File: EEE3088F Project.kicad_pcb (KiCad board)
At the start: 2 copper layers, 56 parts, among them J1 Conn_02x16_Odd_Even, J2 Battery IN JST, J3 USB_C_Receptacle_PowerOnly_24P, M1Control1 DRV8837, M2Control1 DRV8837, M3Control1 DRV8837, M4Control1 DRV8837, Q1 AO3400A, U1 TP4056-42-ESOP8, U2 TPS62160DGK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

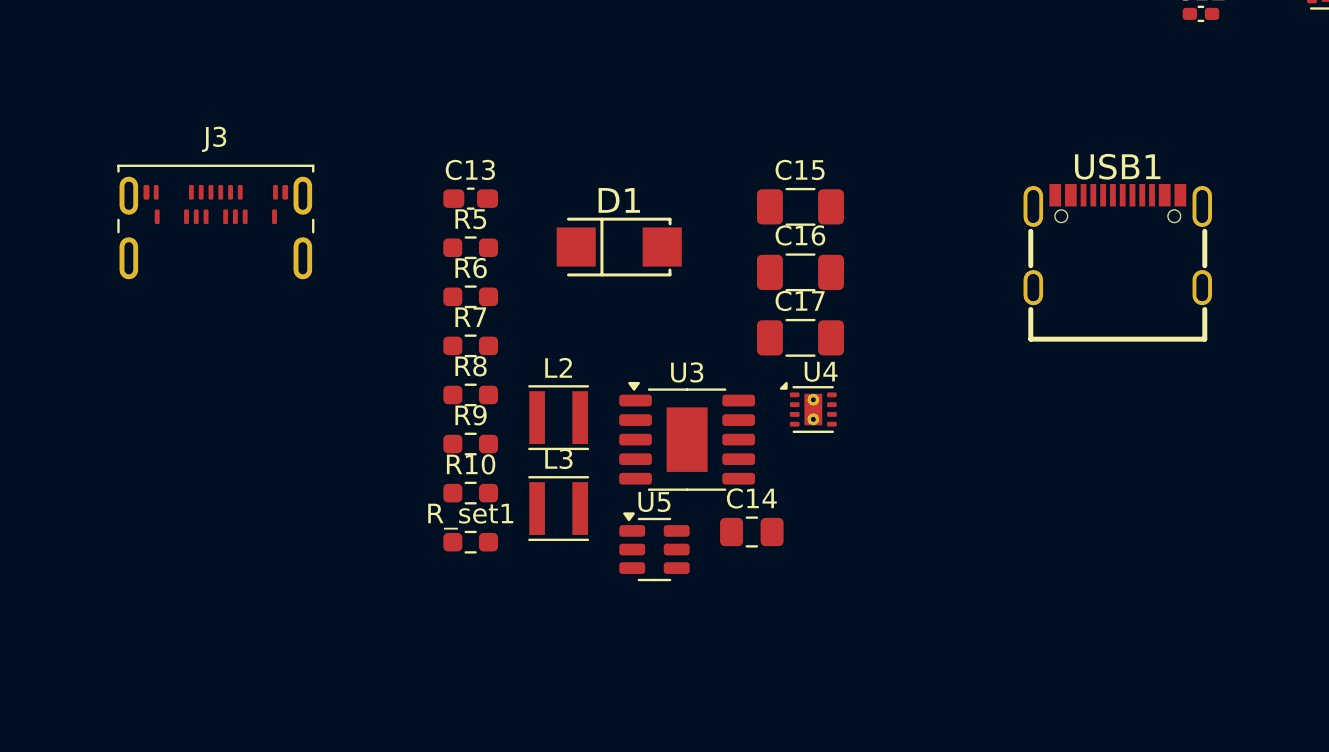
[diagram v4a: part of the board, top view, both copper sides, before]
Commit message: added custom symbol and placed usbc and schottky custom footprints into custom footprints.pretty
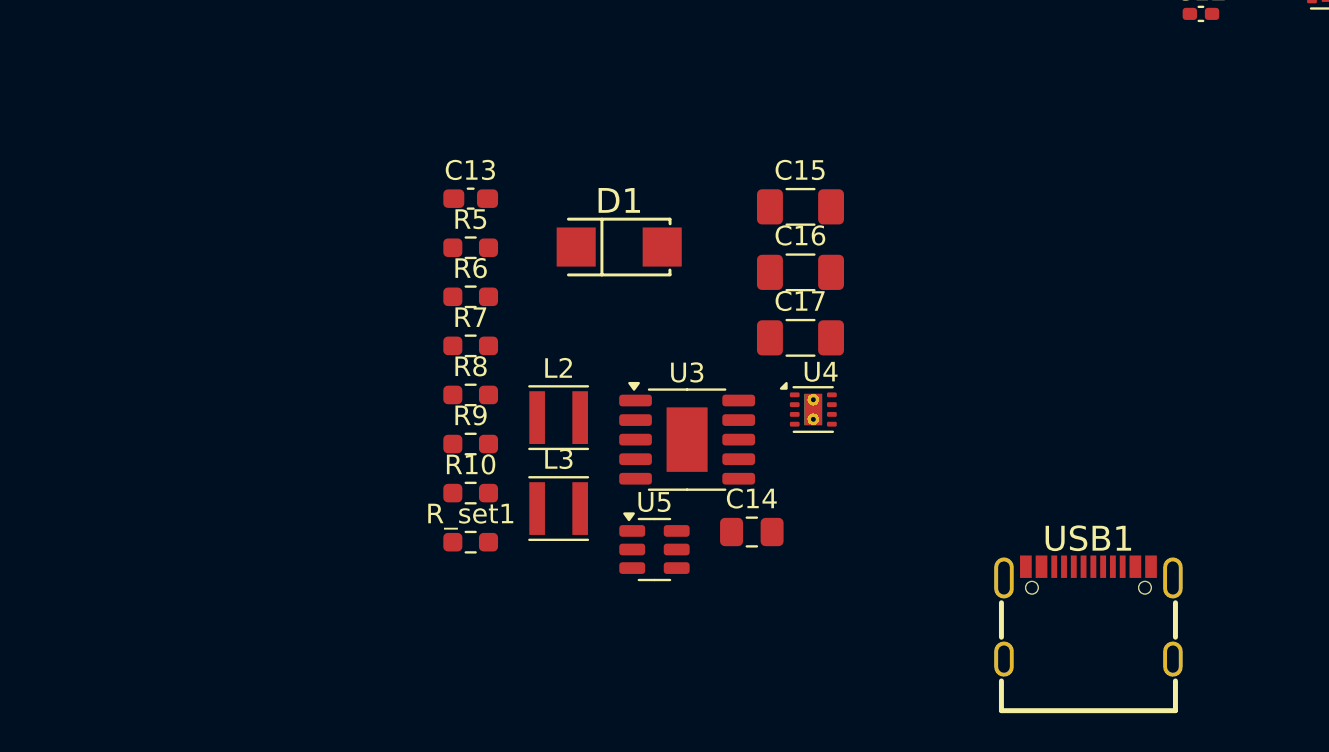
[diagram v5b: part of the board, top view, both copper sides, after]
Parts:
- removed J3: USB_C_Receptacle_PowerOnly_24P, Connector_USB:USB_C_Receptacle_Amphenol_124019772112A
- D1: footprint SMA_L4.3-W2.6-LS5.2-RD:SMA_L4.3-W2.6-LS5.2-RD -> Custom Footprints:SMA_L4.3-W2.6-LS5.2-RD
- USB1: footprint TYPE-C16PIN__:USB-C-SMD_TYPE-C16PIN -> Custom Footprints:USB-C-SMD_TYPE-C16PIN
- moved USB1 19.1 mm to (128.2, 128.6)

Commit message: Cleaned up battery charging circuit and added Battery, 3V3_out and 5V_out labels to motherboard connection
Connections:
- net Net-(R5-Pad1) renamed /VBUS_USBC
- net Net-(U3-CC1) renamed /CC1
- net Net-(U3-CC2) renamed /CC2
- C14 pad 1: 5V -> /5V_out
- C15 pad 1: 3V3 -> /3V3_out
- C17 pad 1: 5V -> /5V_out
- D1 pad 1: 5V -> /5V_out
- J1 pad 14: unconnected-(J1-Pin_14-Pad14) -> VBatt
- J1 pad 18: unconnected-(J1-Pin_18-Pad18) -> /3V3_out
- J1 pad 20: unconnected-(J1-Pin_20-Pad20) -> /5V_out
- L2 pad 2: 3V3 -> /3V3_out
- R7 pad 2: 3V3 -> /3V3_out
- R9 pad 1: 5V -> /5V_out
- U4 pad 2: 5V -> /5V_out
- U4 pad 3: 5V -> /5V_out
- U4 pad 6: 3V3 -> /3V3_out
- USB1 pad 1: unconnected-(USB1-SHELL-Pad1) -> GND
- USB1 pad 2: unconnected-(USB1-SHELL-Pad2) -> GND
- USB1 pad 3: unconnected-(USB1-SHELL-Pad3) -> GND
- USB1 pad 4: unconnected-(USB1-SHELL-Pad4) -> GND
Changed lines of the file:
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@@
 	(net 35 "/FAST_CHRG_CNTRL")
 	(net 36 "Net-(D2-A)")
-	(net 37 "unconnected-(J1-Pin_14-Pad14)")
-	(net 38 "unconnected-(J1-Pin_20-Pad20)")
+	(net 37 "/5V_out")
+	(net 38 "/3V3_out")
 	(net 39 "unconnected-(J1-Pin_12-Pad12)")
 	(net 40 "unconnected-(J1-Pin_25-Pad25)")
 	(net 41 "unconnected-(J1-Pin_22-Pad22)")
 	(net 42 "unconnected-(J1-Pin_21-Pad21)")
-	(net 43 "unconnected-(J1-Pin_18-Pad18)")
+	(net 43 "/VBUS_USBC")
 	(net 44 "unconnected-(J1-Pin_19-Pad19)")
 	(net 45 "unconnected-(J1-Pin_15-Pad15)")
@@
 	(net 53 "VBUS")
 	(net 54 "Net-(U3-VDD)")
-	(net 55 "5V")
-	(net 56 "3V3")
+	(net 55 "/CC2")
+	(net 56 "/CC1")
 	(net 57 "Net-(U4-SW)")
 	(net 58 "Net-(D1-A)")
@@
 	(net 68 "unconnected-(U3-DP-Pad4)")
 	(net 69 "unconnected-(U5-NC-Pad6)")
-	(net 70 "Net-(R5-Pad1)")
-	(net 71 "Net-(U3-CC2)")
-	(net 72 "Net-(U3-CC1)")
-	(net 73 "unconnected-(USB1-SBU1-PadA8)")
-	(net 74 "unconnected-(USB1-DP2-PadB6)")
-	(net 75 "unconnected-(USB1-SBU2-PadB8)")
-	(net 76 "unconnected-(USB1-DN2-PadB7)")
-	(net 77 "unconnected-(USB1-SHELL-Pad3)")
-	(net 78 "unconnected-(USB1-DP1-PadA6)")
-	(net 79 "unconnected-(USB1-DN1-PadA7)")
-	(net 80 "unconnected-(USB1-SHELL-Pad4)")
-	(net 81 "unconnected-(USB1-SHELL-Pad2)")
-	(net 82 "unconnected-(USB1-SHELL-Pad1)")
+	(net 70 "unconnected-(USB1-SBU1-PadA8)")
+	(net 71 "unconnected-(USB1-DP2-PadB6)")
+	(net 72 "unconnected-(USB1-SBU2-PadB8)")
+	(net 73 "unconnected-(USB1-DN2-PadB7)")
+	(net 74 "unconnected-(USB1-DP1-PadA6)")
+	(net 75 "unconnected-(USB1-DN1-PadA7)")
 	(footprint "Package_TO_SOT_SMD:SOT-23"
 		(layer "F.Cu")
@@
 			(layers "F.Cu" "F.Mask" "F.Paste")
 			(roundrect_rratio 0.25)
-			(net 71 "Net-(U3-CC2)")
+			(net 55 "/CC2")
 			(pinfunction "CC2")
 			(pintype "bidirectional")
@@
 			(layers "F.Cu" "F.Mask" "F.Paste")
 			(roundrect_rratio 0.25)
-			(net 72 "Net-(U3-CC1)")
+			(net 56 "/CC1")
 			(pinfunction "CC1")
 			(pintype "bidirectional")
@@
 			(layers "F.Cu" "F.Mask" "F.Paste")
 			(roundrect_rratio 0.25)
-			(net 56 "3V3")
+			(net 38 "/3V3_out")
 			(pintype "passive")
 		)
@@
 			(layers "F.Cu" "F.Mask" "F.Paste")
 			(roundrect_rratio 0.25)
-			(net 55 "5V")
+			(net 37 "/5V_out")
 			(pinfunction "VIN")
 			(pintype "power_in")
@@
 			(layers "F.Cu" "F.Mask" "F.Paste")
 			(roundrect_rratio 0.25)
-			(net 55 "5V")
+			(net 37 "/5V_out")
 			(pinfunction "EN")
 			(pintype "input")
@@
 			(layers "F.Cu" "F.Mask" "F.Paste")
 			(roundrect_rratio 0.25)
-			(net 56 "3V3")
+			(net 38 "/3V3_out")
 			(pinfunction "VOS")
 			(pintype "input")
@@
 			(layers "F.Cu" "F.Mask" "F.Paste")
 			(roundrect_rratio 0.188679)
-			(net 55 "5V")
+			(net 37 "/5V_out")
 			(pintype "passive")
 		)
@@
 			(size 2 2)
 			(layers "F.Cu" "F.Mask" "F.Paste")
-			(net 55 "5V")
+			(net 37 "/5V_out")
 			(pinfunction "K")
 			(pintype "passive")
@@
 			(size 0.8 2.7)
 			(layers "F.Cu" "F.Mask" "F.Paste")
-			(net 56 "3V3")
+			(net 38 "/3V3_out")
 			(pinfunction "2")
 			(pintype "passive")
@@
 			(layers "*.Cu" "*.Mask")
 			(remove_unused_layers no)
-			(net 37 "unconnected-(J1-Pin_14-Pad14)")
+			(net 3 "VBatt")
 			(pinfunction "Pin_14")
 			(pintype "passive")
@@
 			(layers "*.Cu" "*.Mask")
 			(remove_unused_layers no)
-			(net 43 "unconnected-(J1-Pin_18-Pad18)")
+			(net 38 "/3V3_out")
 			(pinfunction "Pin_18")
 			(pintype "passive")
@@
 			(layers "*.Cu" "*.Mask")
 			(remove_unused_layers no)
-			(net 38 "unconnected-(J1-Pin_20-Pad20)")
+			(net 37 "/5V_out")
 			(pinfunction "Pin_20")
 			(pintype "passive")
@@
 			(layers "F.Cu" "F.Mask" "F.Paste")
 			(roundrect_rratio 0.212766)
-			(net 55 "5V")
+			(net 37 "/5V_out")
 			(pintype "passive")
 		)
@@
 			(layers "F.Cu" "F.Mask" "F.Paste")
 			(roundrect_rratio 0.25)
-			(net 55 "5V")
+			(net 37 "/5V_out")
 			(pintype "passive")
 		)
@@
 			(layers "F.Cu" "F.Mask" "F.Paste")
 			(roundrect_rratio 0.25)
-			(net 70 "Net-(R5-Pad1)")
+			(net 43 "/VBUS_USBC")
 			(pintype "passive")
 		)
@@
 			(layers "F.Cu" "F.Mask" "F.Paste")
 			(roundrect_rratio 0.188679)
-			(net 56 "3V3")
+			(net 38 "/3V3_out")
 			(pintype "passive")
 		)
@@
 			(layers "*.Cu" "*.Mask")
 			(remove_unused_layers no)
-			(net 82 "unconnected-(USB1-SHELL-Pad1)")
+			(net 1 "GND")
 			(pinfunction "SHELL")
 			(pintype "unspecified")
@@
 			(layers "*.Cu" "*.Mask")
 			(remove_unused_layers no)
-			(net 81 "unconnected-(USB1-SHELL-Pad2)")
+			(net 1 "GND")
 			(pinfunction "SHELL")
 			(pintype "unspecified")
@@
 			(layers "*.Cu" "*.Mask")
 			(remove_unused_layers no)
-			(net 77 "unconnected-(USB1-SHELL-Pad3)")
+			(net 1 "GND")
 			(pinfunction "SHELL")
 			(pintype "unspecified")
@@
 			(layers "*.Cu" "*.Mask")
 			(remove_unused_layers no)
-			(net 80 "unconnected-(USB1-SHELL-Pad4)")
+			(net 1 "GND")
 			(pinfunction "SHELL")
 			(pintype "unspecified")
@@
 			(size 0.6 1.15)
 			(layers "F.Cu" "F.Mask" "F.Paste")
-			(net 70 "Net-(R5-Pad1)")
+			(net 43 "/VBUS_USBC")
 			(pinfunction "VBUS")
 			(pintype "unspecified")
@@
 			(size 0.3 1.15)
 			(layers "F.Cu" "F.Mask" "F.Paste")
-			(net 72 "Net-(U3-CC1)")
+			(net 56 "/CC1")
 			(pinfunction "CC1")
 			(pintype "unspecified")
@@
 			(size 0.3 1.15)
 			(layers "F.Cu" "F.Mask" "F.Paste")
-			(net 78 "unconnected-(USB1-DP1-PadA6)")
+			(net 74 "unconnected-(USB1-DP1-PadA6)")
 			(pinfunction "DP1")
 			(pintype "unspecified")
@@
 			(size 0.3 1.15)
 			(layers "F.Cu" "F.Mask" "F.Paste")
-			(net 79 "unconnected-(USB1-DN1-PadA7)")
+			(net 75 "unconnected-(USB1-DN1-PadA7)")
 			(pinfunction "DN1")
 			(pintype "unspecified")
@@
 			(size 0.3 1.15)
 			(layers "F.Cu" "F.Mask" "F.Paste")
-			(net 73 "unconnected-(USB1-SBU1-PadA8)")
+			(net 70 "unconnected-(USB1-SBU1-PadA8)")
 			(pinfunction "SBU1")
 			(pintype "unspecified")
@@
 			(size 0.6 1.15)
 			(layers "F.Cu" "F.Mask" "F.Paste")
-			(net 70 "Net-(R5-Pad1)")
+			(net 43 "/VBUS_USBC")
 			(pinfunction "VBUS")
 			(pintype "unspecified")
@@
 			(size 0.3 1.15)
 			(layers "F.Cu" "F.Mask" "F.Paste")
-			(net 71 "Net-(U3-CC2)")
+			(net 55 "/CC2")
 			(pinfunction "CC2")
 			(pintype "unspecified")
@@
 			(size 0.3 1.15)
 			(layers "F.Cu" "F.Mask" "F.Paste")
-			(net 74 "unconnected-(USB1-DP2-PadB6)")
+			(net 71 "unconnected-(USB1-DP2-PadB6)")
 			(pinfunction "DP2")
 			(pintype "unspecified")
@@
 			(size 0.3 1.15)
 			(layers "F.Cu" "F.Mask" "F.Paste")
-			(net 76 "unconnected-(USB1-DN2-PadB7)")
+			(net 73 "unconnected-(USB1-DN2-PadB7)")
 			(pinfunction "DN2")
 			(pintype "unspecified")
@@
 			(size 0.3 1.15)
 			(layers "F.Cu" "F.Mask" "F.Paste")
-			(net 75 "unconnected-(USB1-SBU2-PadB8)")
+			(net 72 "unconnected-(USB1-SBU2-PadB8)")
 			(pinfunction "SBU2")
 			(pintype "unspecified")

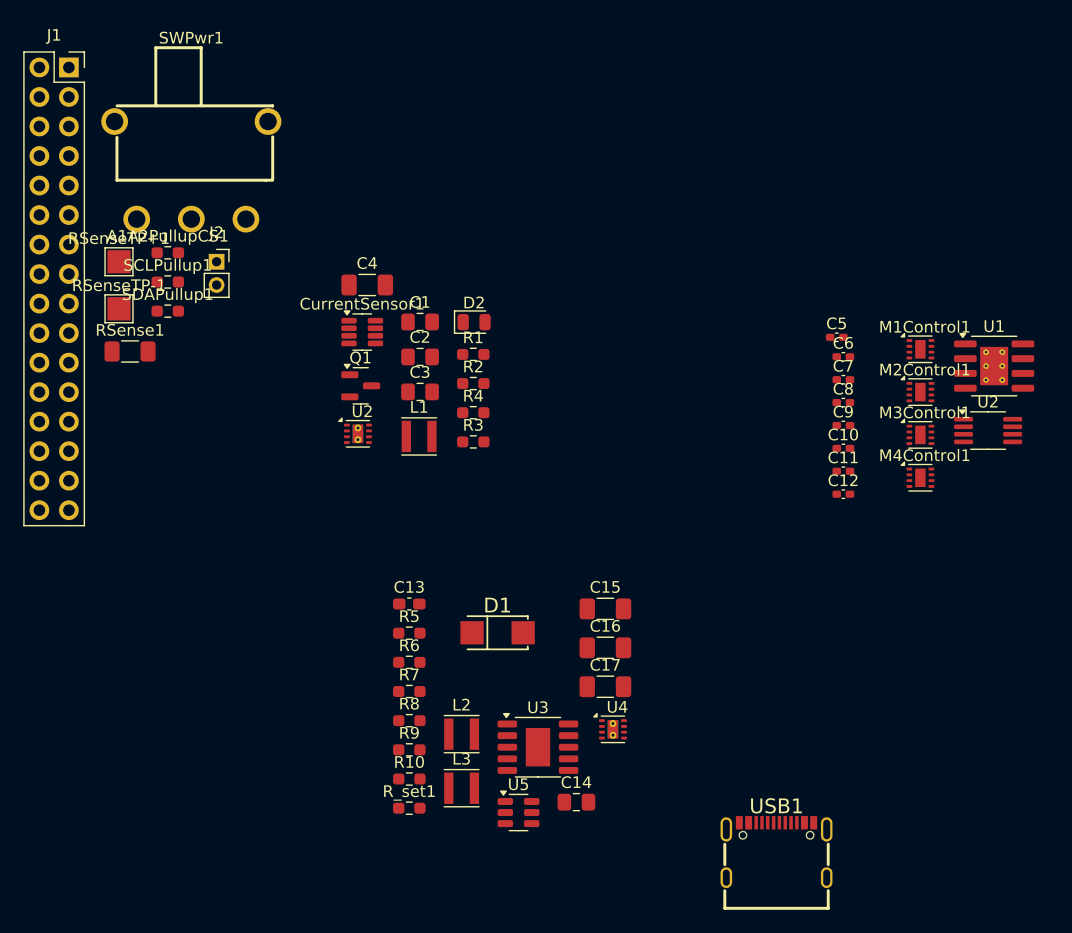
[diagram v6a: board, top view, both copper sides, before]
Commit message: checked footprints and finished BOM for my components
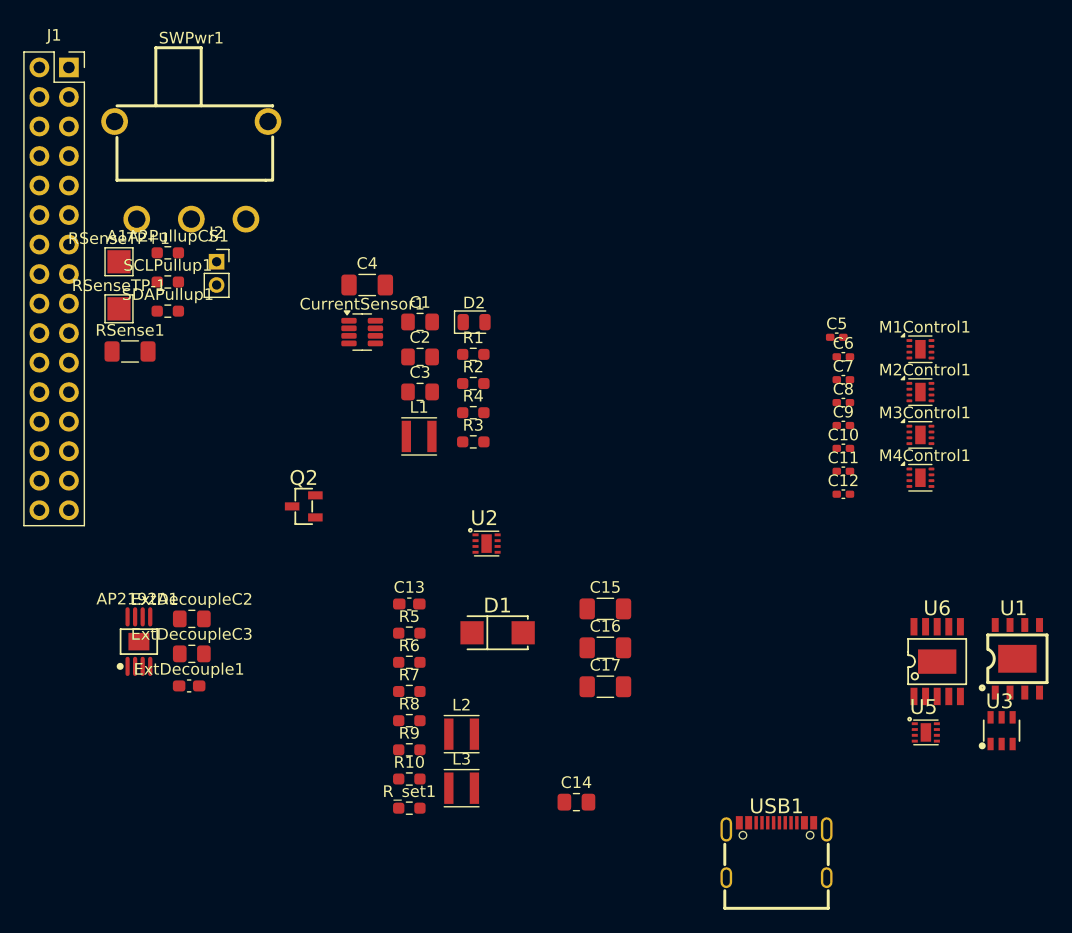
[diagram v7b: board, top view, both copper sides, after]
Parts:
- removed Q1: AO3400A, Package_TO_SOT_SMD:SOT-23
- removed the U2 at (146.4, 92.5)
- removed U4: TPS62162DSG, Package_SON:WSON-8-1EP_2x2mm_P0.5mm_EP0.9x1.6mm_ThermalVias
- added AP2192A1: ~, Custom Footprints:MSOP-8_L3.0-W3.0-P0.65-LS4.9-BL-EP1.8, F.Cu at (73.3, 110.7)
- added ExtDecouple1: 1uF, Capacitor_SMD:C_0603_1608Metric_Pad1.08x0.95mm_HandSolder, F.Cu at (77.6, 114.5)
- added ExtDecoupleC2: 10uF, Capacitor_SMD:C_0805_2012Metric_Pad1.18x1.45mm_HandSolder, F.Cu at (77.9, 108.7)
- added ExtDecoupleC3: 10uF, Capacitor_SMD:C_0805_2012Metric_Pad1.18x1.45mm_HandSolder, F.Cu at (77.9, 111.7)
- added Q2: AO3400A, Custom Footprints:SOT-23-3_L2.9-W1.3-P1.90-LS2.4-BR, F.Cu at (87.5, 99.0)
- added U6: CH224K, Custom Footprints:ESSOP-10_L4.9-W3.9-P1.0-LS6.0-TL-EP, F.Cu at (142.0, 112.4)
- U1: value TP4056-42-ESOP8 -> TP4056; footprint Package_SO:SOIC-8-1EP_3.9x4.9mm_P1.27mm_EP2.41x3.3mm_ThermalVias -> Custom Footprints:ESOP-8_L4.9-W3.9-P1.27-LS6.0-BL-EP
- U2: footprint Package_SON:WSON-8-1EP_2x2mm_P0.5mm_EP0.9x1.6mm_ThermalVias -> Custom Footprints:WSON-8_L2.0-W2.0-P0.50-TL-EP
- U3: value CH224K -> MT3608; footprint Package_SO:SSOP-10-1EP_3.9x4.9mm_P1mm_EP2.1x3.3mm -> Custom Footprints:SOT-23-6_L2.9-W1.6-P0.95-LS2.8-BL
- U5: value MT3608 -> TPS62162DSG; footprint Package_TO_SOT_SMD:SOT-23-6 -> Custom Footprints:WSON-8_L2.0-W2.0-P0.50-TL-EP
- moved U3 39.9 mm to (147.6, 118.4)
- moved U5 35.7 mm to (141.0, 118.5)
- moved U1 25.3 mm to (148.9, 112.2)
- moved U2 14.5 mm to (103.2, 102.2)
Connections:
- C10 pad 1: VBatt -> Net-(JP2-B)
- C11 pad 2: VBatt -> Net-(JP2-B)
- C12 pad 1: VBatt -> Net-(JP2-B)
- C13 pad 1: Net-(U3-VDD) -> Net-(U6-VDD)
- C5 pad 1: VBatt -> Net-(JP2-B)
- C6 pad 2: VBatt -> Net-(JP2-B)
- C7 pad 2: VBatt -> Net-(JP2-B)
- C8 pad 1: VBatt -> Net-(JP2-B)
- C9 pad 2: VBatt -> Net-(JP2-B)
- CurrentSensor1 pad 4: VBatt -> Net-(CurrentSensor1-VS)
- J1 pad 11: /FAST_CHRG_CNTRL -> /EXT_LOAD2_OUT
- J1 pad 13: unconnected-(J1-Pin_13-Pad13) -> /FAST_CHRG_CNTRL
- J1 pad 21: unconnected-(J1-Pin_21-Pad21) -> /EXT_LOAD1_OUT
- J1 pad 25: unconnected-(J1-Pin_25-Pad25) -> /CTRL_EXT_LOAD1
- J1 pad 7: unconnected-(J1-Pin_7-Pad7) -> /CTRL_EXT_LOAD2
- L2 pad 1: Net-(U4-SW) -> Net-(U5-SW)
- M1Control1 pad 1: VBatt -> Net-(JP2-B)
- M1Control1 pad 8: VBatt -> Net-(JP2-B)
- M2Control1 pad 1: VBatt -> Net-(JP2-B)
- M2Control1 pad 8: VBatt -> Net-(JP2-B)
- M3Control1 pad 1: VBatt -> Net-(JP2-B)
- M3Control1 pad 8: VBatt -> Net-(JP2-B)
- M4Control1 pad 1: VBatt -> Net-(JP2-B)
- M4Control1 pad 8: VBatt -> Net-(JP2-B)
- R5 pad 2: Net-(U3-VDD) -> Net-(U6-VDD)
- R6 pad 1: Net-(U3-VBUS) -> VBUS
- R6 pad 2: VBUS -> Net-(U6-VBUS)
- R7 pad 1: Net-(U4-PG) -> Net-(U5-PG)
- R8 pad 1: Net-(U5-FB) -> Net-(U3-FB)
- R9 pad 2: Net-(U5-FB) -> Net-(U3-FB)
- R_set1 pad 1: Net-(U3-CFG1) -> Net-(U6-CFG1)
- SCLPullup1 pad 1: VBatt -> Net-(CurrentSensor1-VS)
- SDAPullup1 pad 1: VBatt -> Net-(CurrentSensor1-VS)
- SWPwr1 pad 3: unconnected-(SWPwr1-C-Pad3) -> Net-(SWPwr1-C)
- U3 pad 1: Net-(U3-VDD) -> Net-(D1-A)
- U3 pad 2: unconnected-(U3-CFG2-Pad2) -> GND
- U3 pad 3: unconnected-(U3-CFG3-Pad3) -> Net-(U3-FB)
- U3 pad 4: unconnected-(U3-DP-Pad4) -> VBatt
- U3 pad 5: unconnected-(U3-DM-Pad5) -> VBatt
- U3 pad 6: /CC2 -> unconnected-(U3-NC-Pad6)
- U5 pad 1: Net-(D1-A) -> GND
- U5 pad 2: GND -> /5V_out
- U5 pad 3: Net-(U5-FB) -> /5V_out
- U5 pad 4: VBatt -> GND
- U5 pad 5: VBatt -> GND
- U5 pad 6: unconnected-(U5-NC-Pad6) -> /3V3_out
